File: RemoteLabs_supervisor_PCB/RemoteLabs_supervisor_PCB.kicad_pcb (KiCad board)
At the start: 2 copper layers, 196 parts, among them J1 Super_Prog_Header, J10 ShiftReg_Header, J11 SPI Student, J12 MCU_Header, J13 USB_B_Mini, J14 ShiftReg_Header, J15 SPI Supervisor, J16 MotorController_PWR_IP, J17 MotorController, J18 DC Motor Output, J19 Stepper Motor Output, J2 WS2821B Header, J20 Servo_A, J21 Servo_B, J22 Thermocouple A, J23 limit_switch_A, J24 limit_switch_B, J25 Optical Encoder, J26 Student_Prog_Header, J27 Analog Buffer, J28 student_PA03, J29 3V3 PWR SRC, J3 XT60_connector_DC_45A_male, J30 12V_DC, J31 5V_DC_RPI, J32 GND_BUS, J33 12V_BUS, J34 5V_P_BUS, J35 5V_D_BUS, J36 3V3_BUS, J4 Strip Lighting, J5 USB_A_Stacked, J6 5V_DC_LED, J7 USB_B_Mini, J8 MCU_Header, J9 Spare Student GPIOs, Q1 IRF5305_PBF, SW1 Stepper_Mode, SW2 Student Reset, SW3 Supervisor Reset, U1 R-78C5.0-1.0, U10 4081, U11 4081, U12 4081, U13 74HC86, U14 74HC86, U15 NCS20074D, U16 NCS20074D, U17 NCS20074D, U18 R-78C5.0-1.0, U19 AD8497, U2 TCYSH14F, U20 74LS07, U21 74LS07, U22 74LS07, U23 TCYSH14F, U3 AMS1117-3.3, U4 ATSAMD21G18A-M, U5 4094, U6 ATSAMD21G18A-M, U7 4094, U8 4069, U9 4081, X1 ASEK-xxxMHz, X2 ASEK-xxxMHz

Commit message: PCB layout
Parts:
- removed JP5, JP8: Xtal/IC, 000_Connectors_Immo:SolderJumper-3_P1.3mm_Bridged12_RoundedPad1.0x1.5mm_NumberLabels
- removed TP4: 5V_SERVO, TestPoint:TestPoint_Pad_D1.5mm
- added JP10: Reset Jumper, 000_Connectors_Immo:SolderJumper-2_P1.3mm_Open_Pad1.0x1.5mm, F.Cu at (104.1, 166.7)
- C17, C7: footprint Capacitor_SMD:C_0805_2012Metric_Pad1.18x1.45mm_HandSolder -> Capacitor_Tantalum_SMD:CP_EIA-2012-12_Kemet-R_Pad1.30x1.05mm_HandSolder
- J1, J26: footprint Connector_PinHeader_2.54mm:PinHeader_1x05_P2.54mm_Vertical -> Connector_Molex:Molex_KK-254_AE-6410-05A_1x05_P2.54mm_Vertical
- J3: value XT60_connector_DC_45A_male -> XT60_60A_male
- moved R26 460.1 mm to (186.7, 356.9)
- moved R28 458.8 mm to (186.7, 359.4)
- moved R29 458.7 mm to (198.8, 360.7), turned to 180 degrees
- moved U21 456.4 mm to (176.3, 356.9)
- moved C40 454.8 mm to (177.5, 350.5), turned to 180 degrees
- moved U20 443.3 mm to (185.2, 346.7)
- moved U22 442.1 mm to (192.7, 356.9)
- moved R30 441.5 mm to (198.8, 355.6), turned to 180 degrees
- moved C38 439.6 mm to (194.5, 350.0), turned to 180 degrees
- moved R27 434.5 mm to (186.7, 354.3)
- moved R31 432.8 mm to (198.8, 358.1), turned to 180 degrees
- moved C14 420.1 mm to (95.1, 176.6), turned to -90 degrees
- moved C39 419.9 mm to (186.7, 340.4), turned to 180 degrees
- moved R40 417.8 mm to (97.3, 176.6), turned to 90 degrees
- moved J9 416.6 mm to (80.8, 188.1), turned to 180 degrees
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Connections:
- C14 pad 1: /Student MCU/HSE_IN -> Net-(JP3-Pad2)
- C15 pad 1: Net-(C15-Pad1) -> Net-(U2-Pad2)
- C23 pad 1: /Supervisor MCU/HSE_IN -> Net-(C23-Pad1)
- C2A1 pad 2: GNDD -> Net-(C2A1-Pad2)
- C2B1 pad 1: GNDD -> Net-(C2A1-Pad2)
- C36 pad 1: Net-(C36-Pad1) -> Net-(X2-Pad3)
- J3 pad S1: (no net) -> unconnected-(J3-PadS1)
- J3 pad S2: (no net) -> unconnected-(J3-PadS2)
- JP6 pad 2: Net-(JP6-Pad2) -> Net-(C23-Pad1)
- R3 pad 1: GNDD -> Net-(C2A1-Pad2)
- R4 pad 1: GNDD -> Net-(C2A1-Pad2)
- R40 pad 1: Net-(C15-Pad1) -> Net-(U2-Pad2)
- R41 pad 1: Net-(C36-Pad1) -> Net-(X2-Pad3)
- U2 pad 2: Net-(JP5-Pad1) -> Net-(U2-Pad2)
- U23 pad 2: Net-(JP8-Pad1) -> Net-(X2-Pad3)
- U4 pad 40: GNDD -> Net-(C2A1-Pad2)
- X1 pad 3: Net-(JP5-Pad2) -> Net-(U2-Pad2)
- X2 pad 1: Net-(JP6-Pad2) -> Net-(C23-Pad1)
- X2 pad 3: Net-(JP8-Pad2) -> Net-(X2-Pad3)
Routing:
- net 3V3_DC_MCU: track 0.00 -> 198.1 mm, vias 0 -> 4
- net /Student MCU/PROG_TX: track 0.00 -> 163.3 mm
- net /Supervisor MCU/PROG_TX: track 0.00 -> 150.5 mm, vias 0 -> 2
- net /Student MCU/PROG_RX: track 0.00 -> 146.7 mm, vias 0 -> 2
- net /Supervisor MCU/PROG_RX: track 0.00 -> 146.2 mm, vias 0 -> 2
- net SERVO_1: track 0.00 -> 127.5 mm, vias 0 -> 2
- net /Supervisor MCU/MCU_RESET: track 0.00 -> 117.1 mm
- net /Student MCU/MCU_RESET: track 0.00 -> 115.4 mm, vias 0 -> 1
- net /Student MCU/SCK: track 0.00 -> 102.2 mm, vias 0 -> 1
- net /Supervisor MCU/SCK: track 0.00 -> 100.6 mm, vias 0 -> 1
- net /Supervisor MCU/LATCH: track 0.00 -> 100.5 mm, vias 0 -> 2
- net /Student MCU/LATCH: track 0.00 -> 92.6 mm, vias 0 -> 2
- net /Student MCU/MOSI: track 0.00 -> 89.8 mm, vias 0 -> 2
- net GNDD: track 0.00 -> 89.4 mm
- net /Supervisor MCU/MOSI: track 0.00 -> 79.2 mm, vias 0 -> 1
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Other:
- copper layers 2 -> 4
- board text added: "ANALOG DISTRIBUTION"
- board text added: "DIGITAL DISTRIBUTION"
- board text removed: "DISTRIBUTION"

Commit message: PCB layout
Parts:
- added H1: MountingHole, MountingHole:MountingHole_3.2mm_M3_Pad_Via, F.Cu at (62.6, 29.0)
- added H2: MountingHole, MountingHole:MountingHole_3.2mm_M3_Pad_Via, F.Cu at (59.8, 117.7)
- added H3: MountingHole, MountingHole:MountingHole_3.2mm_M3_Pad_Via, F.Cu at (210.1, 27.2)
- added H4: MountingHole, MountingHole:MountingHole_3.2mm_M3_Pad_Via, F.Cu at (117.5, 34.3)
- added H5: MountingHole, MountingHole:MountingHole_3.2mm_M3_Pad_Via, F.Cu at (151.4, 116.2)
- added H6: MountingHole, MountingHole:MountingHole_3.2mm_M3_Pad_Via, F.Cu at (215.1, 107.6)
- J19: footprint Connector_PinHeader_2.54mm:PinHeader_1x04_P2.54mm_Vertical -> Connector_JST:JST_XH_B4B-XH-A_1x04_P2.50mm_Vertical
- J2: footprint Connector_PinHeader_2.54mm:PinHeader_1x03_P2.54mm_Vertical -> Connector_Molex:Molex_KK-254_AE-6410-03A_1x03_P2.54mm_Vertical
- J23, J24: footprint Connector_PinHeader_2.54mm:PinHeader_1x02_P2.54mm_Vertical -> Connector_Molex:Molex_KK-254_AE-6410-02A_1x02_P2.54mm_Vertical
- J25: footprint Connector_PinHeader_2.54mm:PinHeader_1x05_P2.54mm_Vertical -> Connector_Molex:Molex_KK-254_AE-6410-05A_1x05_P2.54mm_Vertical
- J4: footprint Connector_PinHeader_1.27mm:PinHeader_1x02_P1.27mm_Vertical -> Connector_Molex:Molex_KK-254_AE-6410-02A_1x02_P2.54mm_Vertical
- moved R17 339.3 mm to (138.4, 36.6), turned to -90 degrees
- moved R19 338.3 mm to (134.0, 36.6), turned to -90 degrees
- moved J25 338.0 mm to (152.5, 26.9)
- moved R21 337.5 mm to (129.5, 36.6), turned to -90 degrees
- moved J24 321.0 mm to (174.1, 26.9)
- moved J23 314.1 mm to (167.3, 26.9)
- moved R20 307.9 mm to (173.4, 38.9), turned to -90 degrees
- moved U21 301.9 mm to (99.2, 65.0)
- moved C40 301.8 mm to (99.1, 59.1)
- moved R18 301.4 mm to (167.4, 38.9), turned to -90 degrees
- moved J3 295.9 mm to (222.0, 119.1), turned to 180 degrees
- moved R26 294.1 mm to (96.9, 76.8)
- moved R28 294.1 mm to (96.9, 79.4)
- moved R29 294.1 mm to (109.0, 80.6)
- moved R30 294.1 mm to (109.0, 75.6)
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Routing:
- net 12V_DC_BUS: track 0.00 -> 240.2 mm
- net USB_BUS: track 0.00 -> 162.9 mm, vias 0 -> 2
- net MODE_1: track 1.62 -> 162.7 mm, vias 0 -> 2
- net 5V_DC_RPI: track 0.00 -> 148.5 mm
- net MODE_2: track 32.8 -> 167.4 mm
- net MODE_0: track 1.62 -> 130.9 mm, vias 0 -> 2
- net /Output Logic/MOTOR_DIR_B: track 20.3 -> 147.5 mm, vias 1 -> 5
- net 5V_DC_LED: track 0.00 -> 118.0 mm, vias 0 -> 1
- net /Output Logic/STUDENT_STEP: track 33.9 -> 148.3 mm, vias 1 -> 2
- net STPPR_FAULT: track 0.00 -> 113.9 mm, vias 0 -> 1
- net /Output Logic/STUDENT_MOTOR_PWM: track 5.69 -> 111.3 mm, vias 0 -> 2
- net /Output Logic/STUDENT_STEP_RST: track 13.7 -> 118.1 mm, vias 0 -> 2
- net 5V_DC_SERVO: track 11.5 -> 115.6 mm, vias 0 -> 1
- net /Output Logic/SUPERVISOR_STEP: track 18.6 -> 117.6 mm, vias 1 -> 4
- net /Digital Sensor Buffers/D_IN_B: track 0.00 -> 98.9 mm, vias 0 -> 2
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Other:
- board outline added: 180.3 x 99.1 mm
- board text removed: "INPUTS"

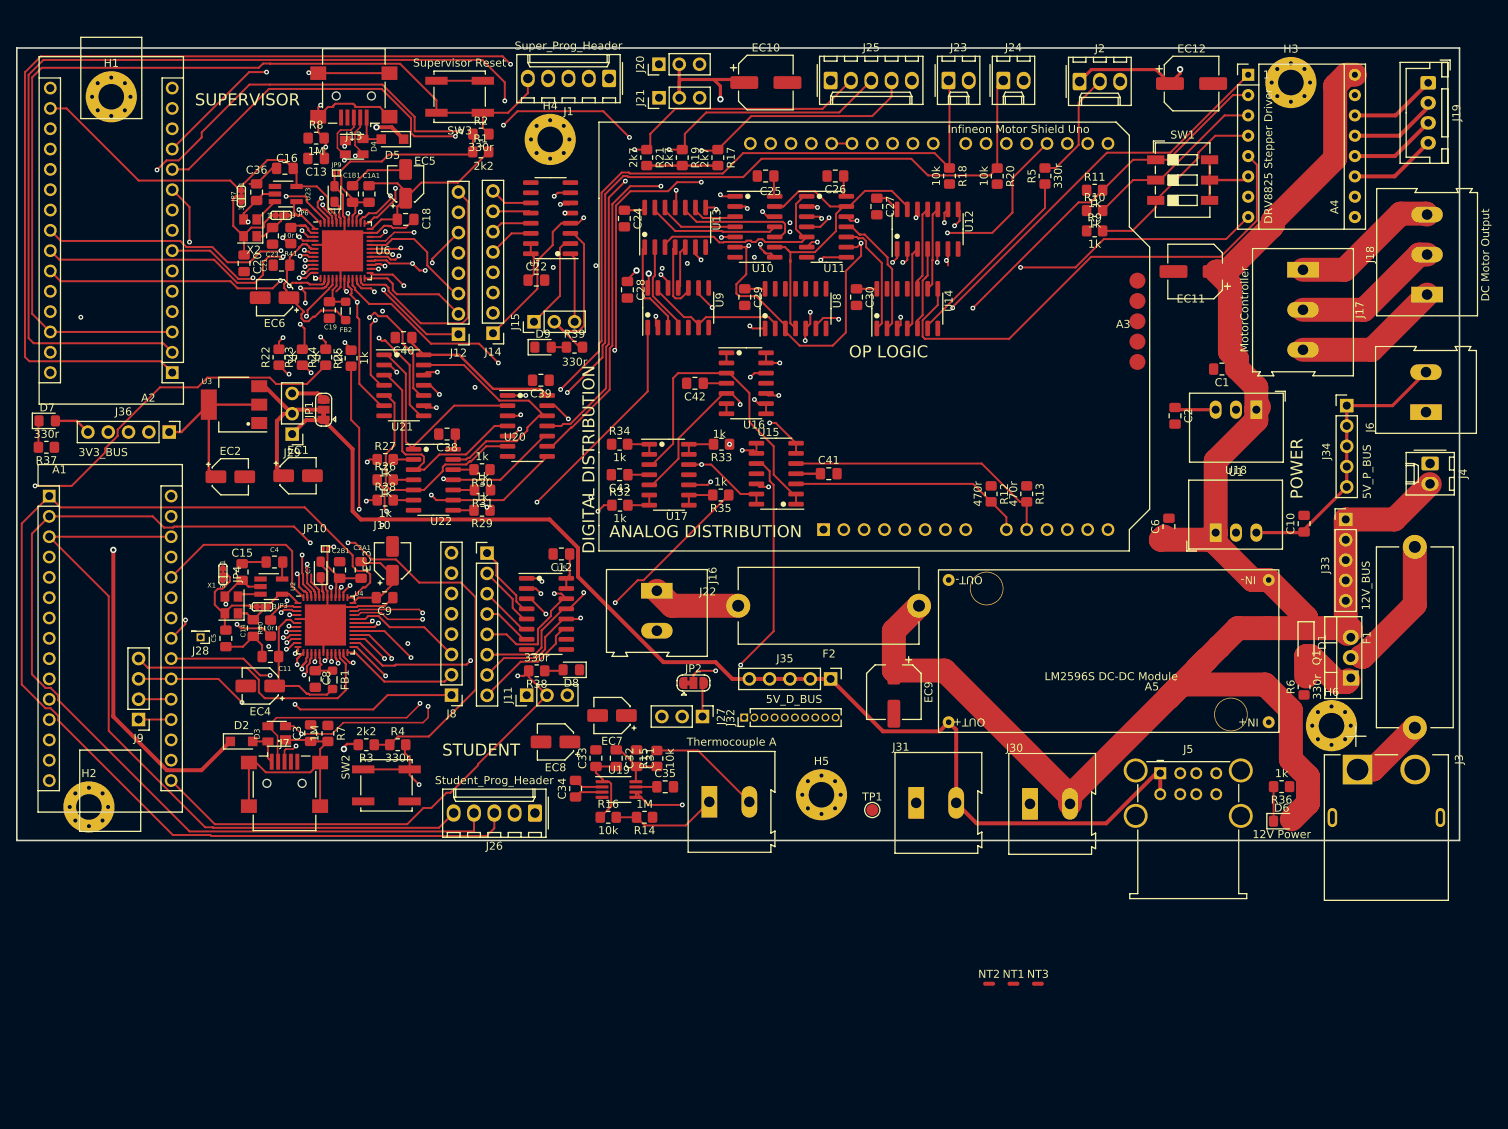
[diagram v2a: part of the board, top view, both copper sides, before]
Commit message: version one finished excluding net ties
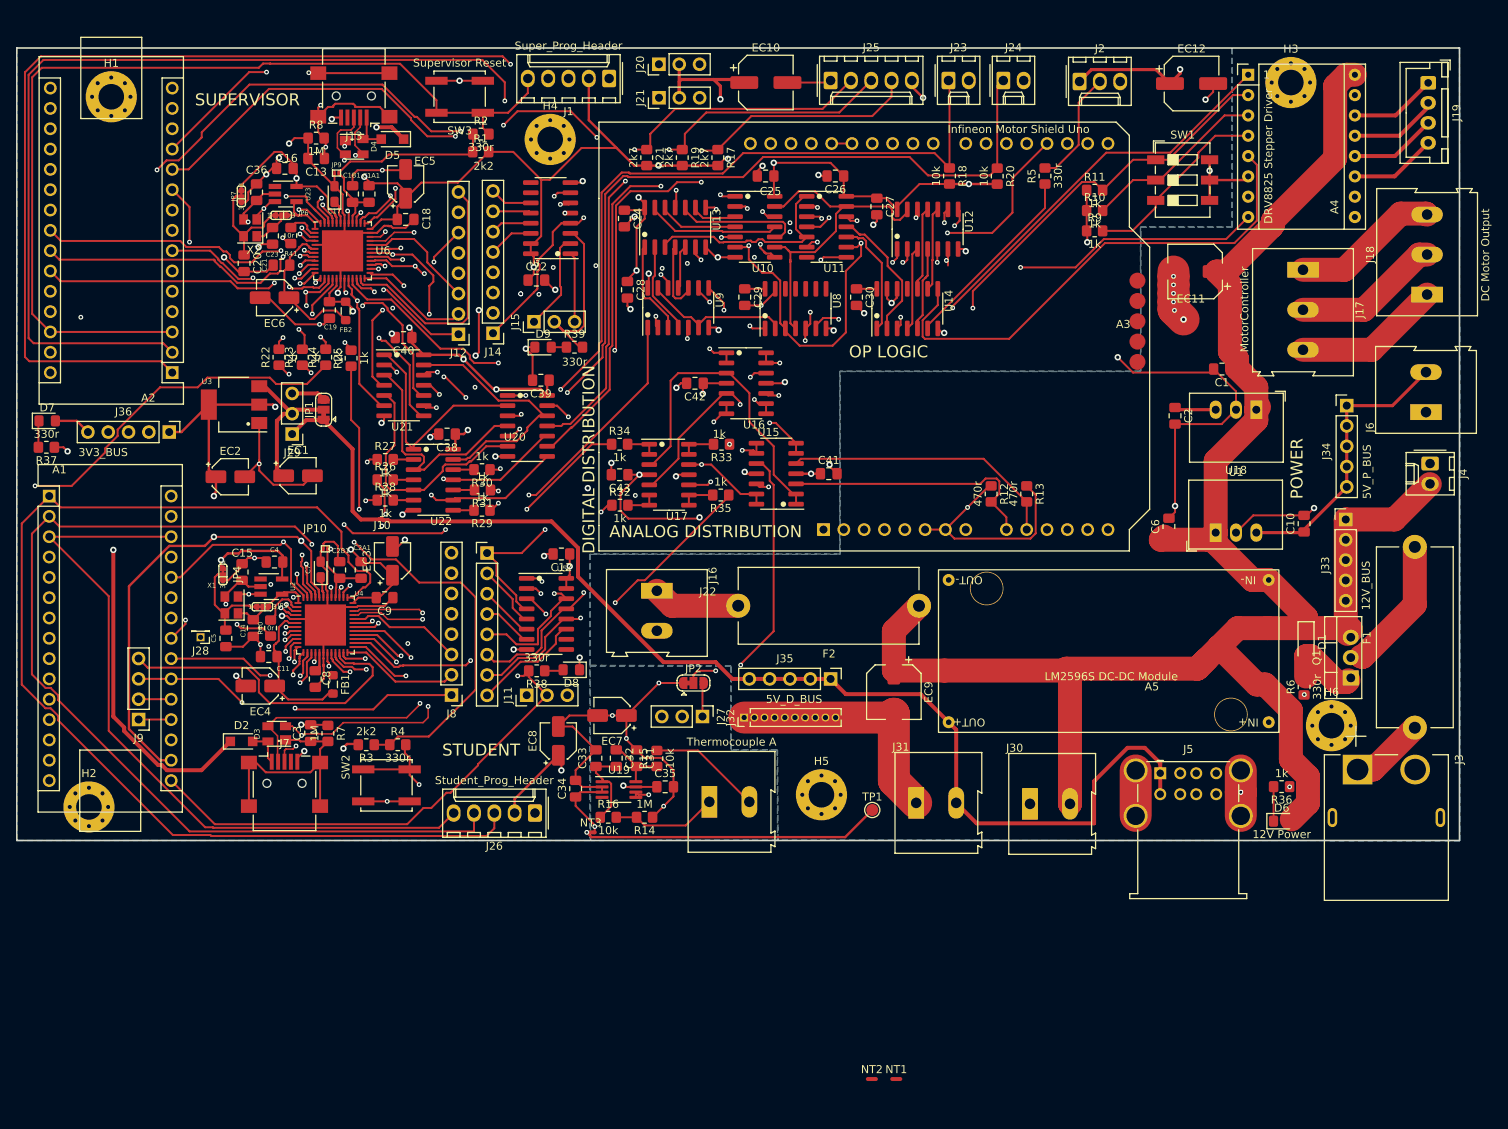
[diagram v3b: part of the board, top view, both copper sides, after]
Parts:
- moved NT3 59.0 mm to (122.5, 120.9)
- moved NT1 18.9 mm to (160.7, 151.7)
- moved NT2 18.9 mm to (157.7, 151.7)
- moved FB1 0.58 mm to (90.3, 102.4)
- moved EC8 0.38 mm to (118.5, 109.5), turned to 90 degrees
- moved C11 0.20 mm to (82.3, 98.9)
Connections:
- C1 pad 2: GNDPWR -> GNDD
- C10 pad 2: GNDPWR -> GNDD
- C2 pad 2: GNDPWR -> GNDD
- C41 pad 2: GNDA -> GNDD
- C42 pad 2: GNDA -> GNDD
- C43 pad 2: GNDA -> GNDD
- C6 pad 2: GNDPWR -> GNDD
- EC1 pad 2: GNDPWR -> GNDD
- EC10 pad 2: GNDPWR -> GNDD
- EC12 pad 2: GNDPWR -> GNDD
- EC2 pad 2: GNDPWR -> GNDD
- J20 pad 3: GNDPWR -> GNDD
- J21 pad 3: GNDPWR -> GNDD
- J6 pad 1: GNDPWR -> GNDD
- R37 pad 1: GNDPWR -> GNDD
- U1 pad 2: GNDPWR -> GNDD
- U15 pad 11: GNDA -> GNDD
- U16 pad 11: GNDA -> GNDD
- U17 pad 11: GNDA -> GNDD
- U18 pad 2: GNDPWR -> GNDD
- U3 pad 1: GNDPWR -> GNDD
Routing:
- net 3V3_DC_MCU: track 236.6 -> 694.5 mm, vias 3 -> 34
- net GNDD: track 89.6 -> 417.2 mm, vias 0 -> 58
- net /Analog Sensor Buffers/A_OUT_A1: track 50.2 -> 116.2 mm, vias 1 -> 5
- net /Analog Sensor Buffers/A_OUT_B1: track 38.0 -> 102.1 mm, vias 2 -> 5
- net /Output Logic/SUPERVISOR_MOTOR_PWM: track 38.7 -> 91.5 mm, vias 1 -> 3
- net GNDA: track 7.50 -> 59.6 mm, vias 0 -> 5
- net GNDPWR: track 0.00 -> 49.1 mm, vias 0 -> 10
- net /Output Logic/STUDENT_MOTOR_EN: track 9.24 -> 58.0 mm, vias 0 -> 2
- net /Analog Sensor Buffers/A_OUT_A2: track 23.5 -> 71.5 mm, vias 0 -> 4
- net STU_STP_FLT: track 42.5 -> 87.4 mm, vias 1 -> 2
- net OE_B: track 47.1 -> 85.1 mm, vias 1 -> 3
- net GND: track 0.00 -> 37.3 mm, vias 0 -> 1
- net /Output Logic/STUDENT_STEP_RST: track 118.1 -> 101.7 mm
- net 5V_DC_SERVO: track 115.6 -> 101.6 mm
- net /Output Logic/STUDENT_DIRECTION: track 76.6 -> 83.6 mm
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- added copper zone on B.Cu, net GNDA
- added copper zone on B.Cu, net GNDD
- added copper zone on B.Cu, net GNDPWR

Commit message: routing board layout 2.0
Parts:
- removed TP1: GND, TestPoint:TestPoint_Pad_D1.5mm
- removed the U12 at (164.7, 45.5)
- added U9: 4081, Package_SO:SOIC-14_3.9x8.7mm_P1.27mm, F.Cu at (144.4, 44.5)
- JP1, JP2: moved to B.Cu
- moved R2 60.4 mm to (52.2, 54.6), turned to -90 degrees
- moved R5 56.7 mm to (122.6, 39.3)
- moved R1 56.7 mm to (52.2, 39.5), turned to 90 degrees
- moved R20 55.1 mm to (118.2, 39.4)
- moved R18 53.8 mm to (113.6, 39.4)
- moved J26 51.2 mm to (83.4, 78.7), turned to -90 degrees
- moved EC9 48.7 mm to (203.8, 81.2)
- moved J1 48.5 mm to (81.3, 48.1), turned to -90 degrees
- moved U16 44.4 mm to (106.2, 91.0)
- moved C42 43.9 mm to (100.3, 91.0)
- moved C18 43.8 mm to (57.7, 57.7), turned to -90 degrees
- moved C1A1 42.8 mm to (52.2, 44.2)
- moved C1B1 41.5 mm to (52.2, 49.9), turned to -90 degrees
- moved C41 40.2 mm to (124.6, 105.2), turned to -90 degrees
- moved JP9 39.6 mm to (52.2, 47.1), turned to -90 degrees
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- renumbered U9 to U12
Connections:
- U10 pad 12: /Output Logic/SUPERVISOR_STEP -> /Output Logic/STUDENT_STEP_RST
- U10 pad 13: Net-(U10-Pad13) -> /Output Logic/MCU_STEP_SELECT
- U10 pad 8: /Output Logic/SUPERVISOR_DIRECTION -> /Output Logic/STUDENT_STEP_EN
- U10 pad 9: Net-(U10-Pad13) -> /Output Logic/MCU_STEP_SELECT
- U11 pad 1: Net-(U11-Pad1) -> /Output Logic/SUPERVISOR_DIRECTION
- U11 pad 12: /Output Logic/SUPERVISOR_STEP_EN -> /Output Logic/SUPERVISOR_STEP_RST
- U11 pad 13: Net-(U10-Pad13) -> Net-(U11-Pad2)
- U11 pad 2: /Output Logic/MOTOR_DIR_A -> Net-(U11-Pad2)
- U11 pad 3: /DC Motor Controller/IN_1 -> Net-(U11-Pad3)
- U11 pad 4: /DC Motor Controller/IN_2 -> Net-(U11-Pad4)
- U11 pad 5: Net-(U11-Pad1) -> /Output Logic/SUPERVISOR_STEP
- U11 pad 6: /Output Logic/MOTOR_DIR_B -> Net-(U11-Pad2)
- U11 pad 8: /Output Logic/STUDENT_STEP_EN -> /Output Logic/SUPERVISOR_STEP_EN
- U11 pad 9: /Output Logic/MCU_STEP_SELECT -> Net-(U11-Pad2)
- U12 pad 10: Net-(U13-Pad4) -> Net-(U12-Pad10)
- U12 pad 11: Net-(U13-Pad5) -> Net-(U12-Pad11)
- U12 pad 12: /Output Logic/SUPERVISOR_MOTOR_EN -> /Output Logic/SUPERVISOR_PIXEL_DATA
- U12 pad 13: Net-(U8-Pad2) -> Net-(U12-Pad13)
- U12 pad 3: Net-(U13-Pad1) -> Net-(U14-Pad1)
- U12 pad 4: Net-(U13-Pad2) -> Net-(U14-Pad4)
- U12 pad 5: /Output Logic/SUPERVISOR_MOTOR_PWM -> /Output Logic/STUDENT_MOTOR_EN
- U12 pad 6: Net-(U8-Pad2) -> /Output Logic/MCU_MOTOR_SELECT
- U12 pad 8: /Output Logic/STUDENT_MOTOR_EN -> /Output Logic/STUDENT_PIXEL_DATA
- U12 pad 9: /Output Logic/MCU_MOTOR_SELECT -> /Output Logic/MCU_PIXEL_SELECT
- U13 pad 1: Net-(U13-Pad1) -> Net-(U10-Pad3)
- U13 pad 10: Net-(U10-Pad10) -> Net-(U11-Pad10)
- U13 pad 11: /Output Logic/STEPP_STEP_OUT -> /Output Logic/STEP_RST_OUT
- U13 pad 12: Net-(U10-Pad4) -> Net-(U10-Pad11)
- U13 pad 13: Net-(U10-Pad11) -> Net-(U11-Pad11)
- U13 pad 2: Net-(U13-Pad2) -> Net-(U11-Pad3)
- U13 pad 3: Net-(U11-Pad1) -> /Output Logic/DIRECTION_OUT
- U13 pad 4: Net-(U13-Pad4) -> Net-(U10-Pad4)
- U13 pad 5: Net-(U13-Pad5) -> Net-(U11-Pad4)
- U13 pad 6: /DC Motor Controller/ENABLE -> /Output Logic/STEPP_STEP_OUT
- U13 pad 8: /Output Logic/DIRECTION_OUT -> /Output Logic/STEP_EN_OUT
- U13 pad 9: Net-(U10-Pad3) -> Net-(U10-Pad10)
- U14 pad 1: Net-(U11-Pad10) -> Net-(U14-Pad1)
- U14 pad 2: Net-(U11-Pad11) -> Net-(U14-Pad2)
- U14 pad 3: /Output Logic/STEP_EN_OUT -> Net-(U9-Pad1)
- U14 pad 4: Net-(U12-Pad3) -> Net-(U14-Pad4)
- U14 pad 6: /Output Logic/PIXEL_DATA_OUT -> /DC Motor Controller/ENABLE
- U14 pad 8: /Output Logic/STEP_RST_OUT -> /Output Logic/PIXEL_DATA_OUT
- U8 pad 4: Net-(U10-Pad13) -> Net-(U11-Pad2)
- U8 pad 6: Net-(U12-Pad6) -> Net-(U12-Pad13)
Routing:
- net 3V3_DC_MCU: track 694.5 -> 33.7 mm, vias 34 -> 1
- net GNDD: track 417.2 -> 60.5 mm, vias 58 -> 5
- net 12V_DC_BUS: track 239.1 -> 0.00 mm
- net USB_BUS: track 163.2 -> 0.00 mm, vias 2 -> 0
- net 5V_DC_RPI: track 154.0 -> 0.00 mm
- net /Output Logic/MOTOR_DIR_B: track 148.0 -> 13.5 mm, vias 5 -> 1
- net 5V_DC_LED: track 118.0 -> 0.00 mm, vias 1 -> 0
- net STPPR_FAULT: track 116.3 -> 0.00 mm, vias 1 -> 0
- net /Supervisor MCU/PROG_TX: track 153.3 -> 43.0 mm, vias 2 -> 1
- net SERVO_1: track 130.2 -> 20.6 mm, vias 2 -> 1
- net /Output Logic/SUPERVISOR_PIXEL_DATA: track 112.9 -> 5.17 mm, vias 3 -> 1
- net /Output Logic/SUPERVISOR_STEP: track 116.9 -> 9.49 mm, vias 4 -> 1
- net /Supervisor MCU/PROG_RX: track 147.8 -> 42.0 mm, vias 2 -> 1
- net /Output Logic/STUDENT_STEP_RST: track 101.7 -> 0.00 mm, vias 2 -> 0
- net 5V_DC_SERVO: track 101.6 -> 0.00 mm, vias 1 -> 0
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- removed copper zone on B.Cu, net GNDA
- removed copper zone on B.Cu, net GNDD
- removed copper zone on B.Cu, net GNDPWR
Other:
- board size 180.3 x 99.1 mm -> 182.6 x 99.2 mm

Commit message: 2 am save
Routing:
- net /Student MCU/DC_MOTOR_DIR1: track 87.3 -> 557.3 mm
- net /Output Logic/STUDENT_MOTOR_PWM: track 19.4 -> 156.1 mm, vias 1 -> 2
- net /Student MCU/LATCH: track 13.0 -> 85.4 mm, vias 1 -> 2
- net STU_STP_FLT: track 20.4 -> 79.1 mm, vias 1 -> 3
- net /Analog Sensor Buffers/A_OUT_C2: track 17.7 -> 74.0 mm, vias 1 -> 4
- net /Student MCU/SCK: track 22.7 -> 68.2 mm, vias 2 -> 3
- net LIMIT_2: track 6.18 -> 50.3 mm, vias 1 -> 2
- net LIMIT_1: track 27.9 -> 64.8 mm, vias 1 -> 2
- net Net-(J8-Pad4): track 2.96 -> 25.7 mm, vias 1 -> 2
- net /Student MCU/SPARE_0: track 31.3 -> 53.7 mm, vias 1 -> 2
- net /Student MCU/MCU_RESET: track 35.7 -> 57.0 mm, vias 0 -> 2
- net Net-(J8-Pad5): track 2.10 -> 22.8 mm, vias 1 -> 2
- net Net-(J8-Pad3): track 7.60 -> 22.9 mm, vias 1 -> 2
- net /Output Logic/STUDENT_DIRECTION: track 0.00 -> 14.7 mm
- net /Output Logic/STUDENT_STEP_EN: track 0.00 -> 14.4 mm
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
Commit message: 2:01 am save going to bed
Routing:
- net /Output Logic/MOTOR_DIR_B: track 13.5 -> 100.6 mm, vias 1 -> 2
- net /Output Logic/SUPERVISOR_MOTOR_PWM: track 25.3 -> 109.6 mm, vias 3 -> 4
- net /Output Logic/MOTOR_DIR_A: track 26.4 -> 104.7 mm, vias 3 -> 4
- net /Supervisor MCU/MOSI: track 15.6 -> 70.2 mm, vias 2 -> 3
- net SERVO_1: track 20.6 -> 67.2 mm
- net /Supervisor MCU/LATCH: track 13.7 -> 57.0 mm, vias 2 -> 4
- net /Analog Sensor Buffers/A_OUT_B2: track 18.0 -> 57.0 mm, vias 1 -> 3
- net /Analog Sensor Buffers/A_OUT_A2: track 8.51 -> 43.0 mm, vias 1 -> 3
- net /Student MCU/MCU_RESET: track 57.0 -> 84.3 mm
- net LIMIT_1: track 64.8 -> 60.1 mm
- net Net-(J8-Pad4): track 25.7 -> 30.2 mm
- net /Analog Sensor Buffers/A_OUT_C2: track 74.0 -> 77.5 mm
- net /Supervisor MCU/SCK: track 78.2 -> 80.6 mm
- net Net-(J12-Pad1): track 30.9 -> 33.3 mm
- net MODE_0: track 145.5 -> 147.6 mm
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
